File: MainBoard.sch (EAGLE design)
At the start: 47 parts, among them U1 STM32F10XRXT6, X1 53261-03, X2 53261-03, X3 53261-03, X4 53261-03, Y1 8MHz, Y2 32.768kHz

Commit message: płytka
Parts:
- removed C1, C14, C2, C3, C4: 100n, rcl:C-EUC0805
- removed C6: 10u, rcl:CPOL-EUSMCA
- removed ETRX357: ETRX357HR, etrx357_logical:ETRX357HR
- removed G1: CR2032V, battery:CR2032V
- removed SW1: (no value), SparkFun-Electromechanical:SW_DIP-2
- removed X1, X2, X3, X4: 53261-03, con-molex:53261-03
- added C22: (no value), rcl:C-EUC0805
- added IC3: (no value), SparkFun-PowerIC:V_REG_LM1117SOT223
- added JP1: (no value), SparkFun-Connectors:M06LONGPADS
- added JP2, JP3: M05X2SHD, SparkFun-Connectors:M05X2SHD
- added JP4: (no value), SparkFun-Connectors:M04LONGPADS
- added JP5, JP6, JP7, JP8: (no value), SparkFun-Connectors:M03LONGPADS
- added LED5, LED7, LED8, LED9: (no value), led:LEDCHIPLED_0805
- added R10, R12, R13, R14: (no value), resistor:R-EU_M0805
- C21: value 100n -> (none)
- LED1, LED2, LED3: device SparkFun-LED (1):LED1206 -> led:LEDCHIPLED_0805
- R6, R7, R8: value 220 -> (none); device rcl:R-EU_M0805 -> resistor:R-EU_M0805
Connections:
- removed net N$11: LED2.C, R8.2
- removed net N$9: LED3.C, R6.2
- removed net RXD: ETRX357.PB2
- removed net TXD: ETRX357.PB1
- new net 5V: C21.1, IC3.IN, JP5.1, JP6.1, JP7.1, JP8.1
- new net A1: JP2.7, U1PORTB_H.PB8
- new net A2: JP2.5, U1PORTB_H.PB9
- new net A3: JP2.9, U1PORTB_L.PB6
- new net A4: JP2.2, U1PORTB_L.PB7
- new net A5: JP2.8, U1PORTC_H.PC8
- new net A6: JP2.10, U1PORTC_H.PC9
- new net A7: JP2.4, U1PORTC_L.PC6
- new net A8: JP2.6, U1PORTC_L.PC7
- new net L1: R7.1, U1PORTB_H.PB12
- new net L2: R8.1, U1PORTC_L.PC1
- new net L4: R10.1, U1PORTA_L.PA1
- new net L6: R12.1, U1PORTC_L.PC2
- new net L7: R13.1, U1PORTC_L.PC3
- new net MISO: JP3.9, U1PORTA_L.PA6
- new net MOSI: JP3.10, U1PORTA_L.PA7
- new net N$12: LED7.A, R12.2
- new net N$13: LED8.A, R13.2
- new net N$14: LED9.A, R14.2
- new net REG1: JP5.3, U1PORTA_H.PA8
- new net REG2: JP6.3, U1PORTA_H.PA9
- new net REG3: JP7.3, U1PORTA_H.PA10
- new net REG4: JP8.3, U1PORTA_H.PA11
- new net RX: JP3.5, U1PORTA_L.PA3
- new net SCK: JP3.8, U1PORTA_L.PA5
- new net SWO: JP1.6
- new net TX: JP3.6, U1PORTA_L.PA2
- net 3.3V: now also C22.1, IC3.OUT, IC3.OUT@1, JP1.1, JP2.1, JP3.2, JP4.2, JP4.3, R14.1, R6.1; no longer C1.1, C14.1, C2.1, C21.1, C3.1, C4.1, C6.+, ETRX357.VCC, SW1.3, SW1.4
- net GND: now also C22.2, IC3.ADJ, JP1.3, JP2.3, JP3.1, JP5.2, JP6.2, JP7.2, JP8.2, LED1.C, LED2.C, LED3.C, LED5.C, LED7.C, LED8.C, LED9.C; no longer C1.2, C14.2, C2.2, C3.2, C4.2, C6.-, ETRX357.GND@1, ETRX357.GND@2, ETRX357.GND@3, ETRX357.GND@4, ETRX357.GND@5, ETRX357.GND@6, G1.-, R6.1, R7.1, R8.1
- net N$1: now also JP4.1; no longer SW1.1
- net N$10: now also LED5.A, R10.2; no longer LED1.C, R7.2
- net N$2: now also JP4.4; no longer SW1.2
- net N$6: now also R6.2; no longer ETRX357.PC6
- net N$7: now also R7.2; no longer ETRX357.PC7
- net N$8: now also R8.2; no longer ETRX357.PB7
- net NRST: now also JP1.5
- net SCL: now also U1PORTB_H.PB10
- net SDA: now also U1PORTB_H.PB11
- net SWCLK: now also JP1.2
- net SWDIO: now also JP1.4
- net V_BATT: no longer G1.+
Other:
- note removed: "BATTERY"
- note removed: "ETRX357 ZigBee"
- note removed: "VDD/VSS"
- moved on the sheet: C21, C5, C7, LED1, LED2, LED3, R6, R7, R8, Y1

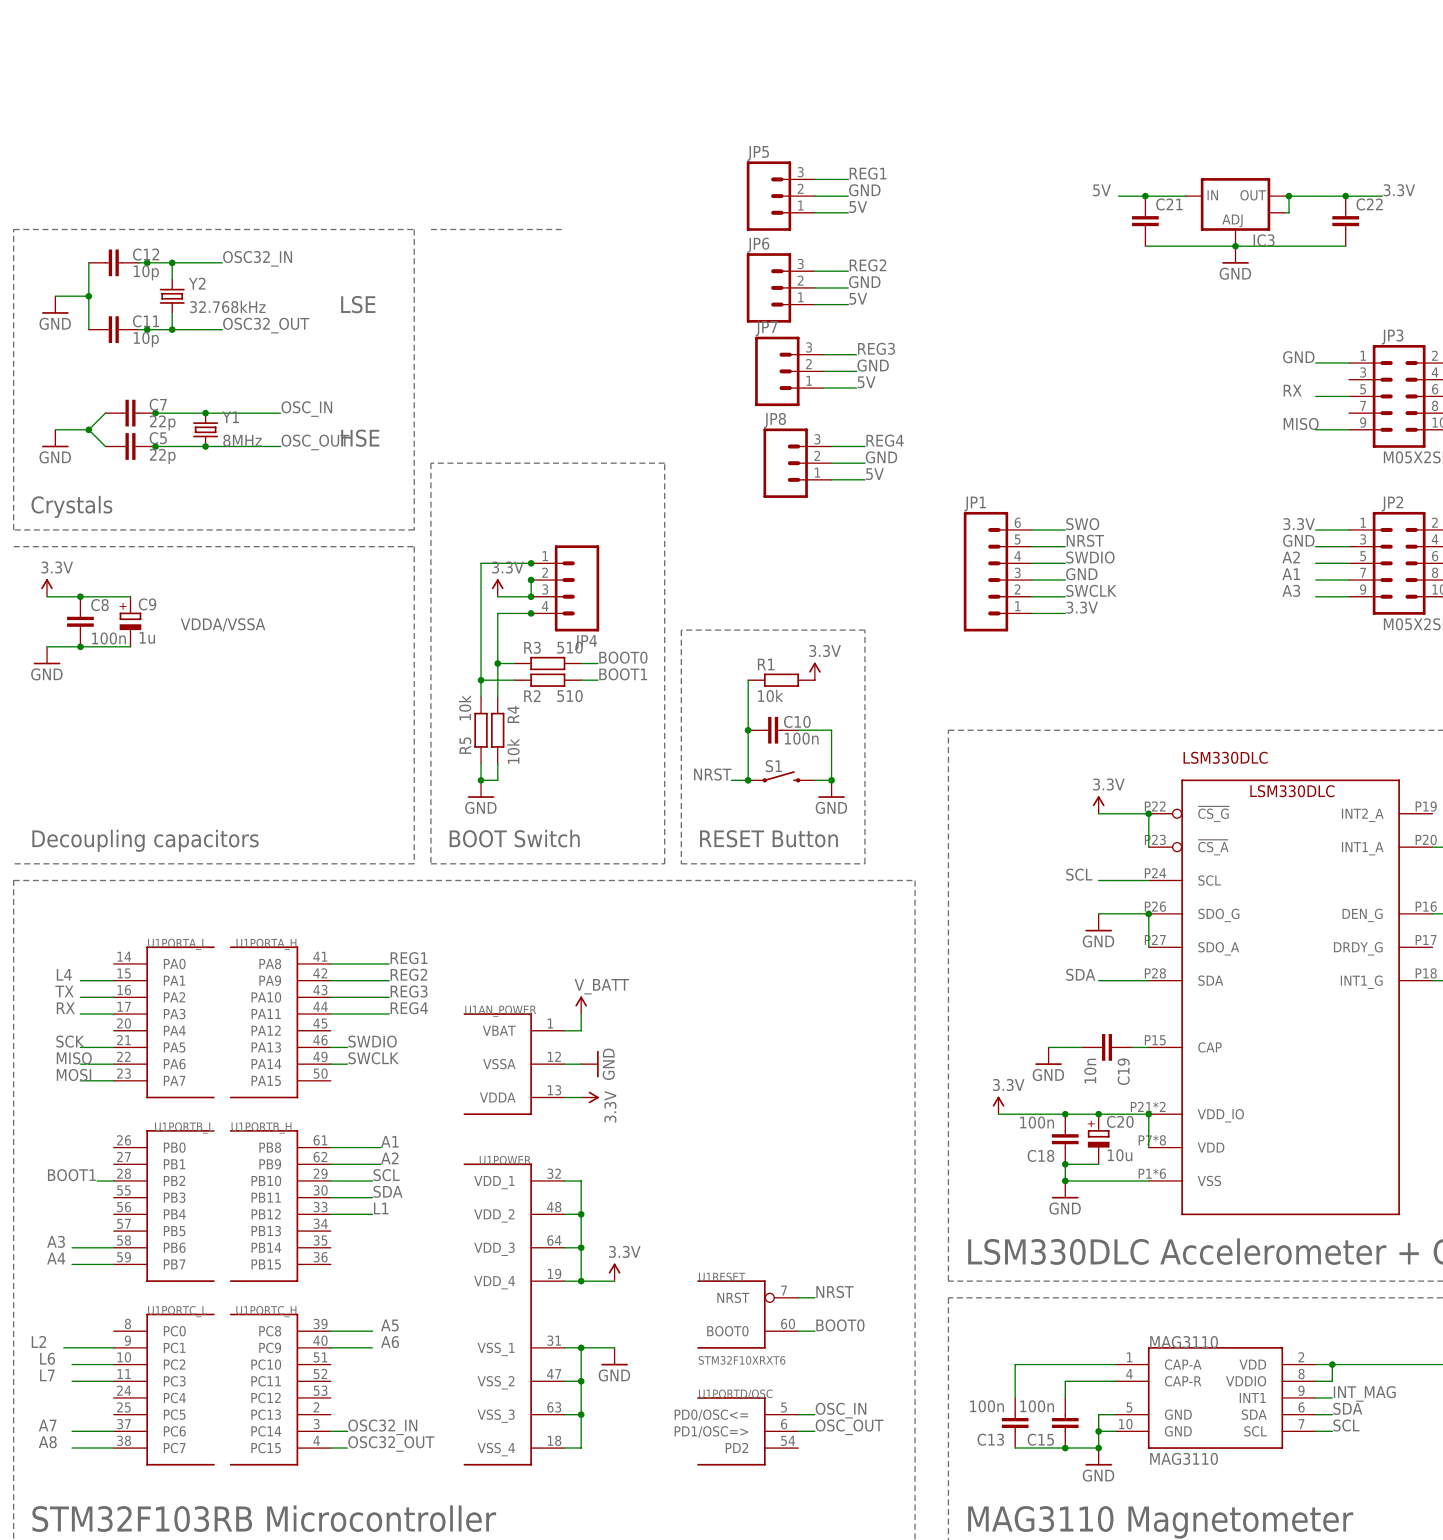
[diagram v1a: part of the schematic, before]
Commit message: buzzer i adc
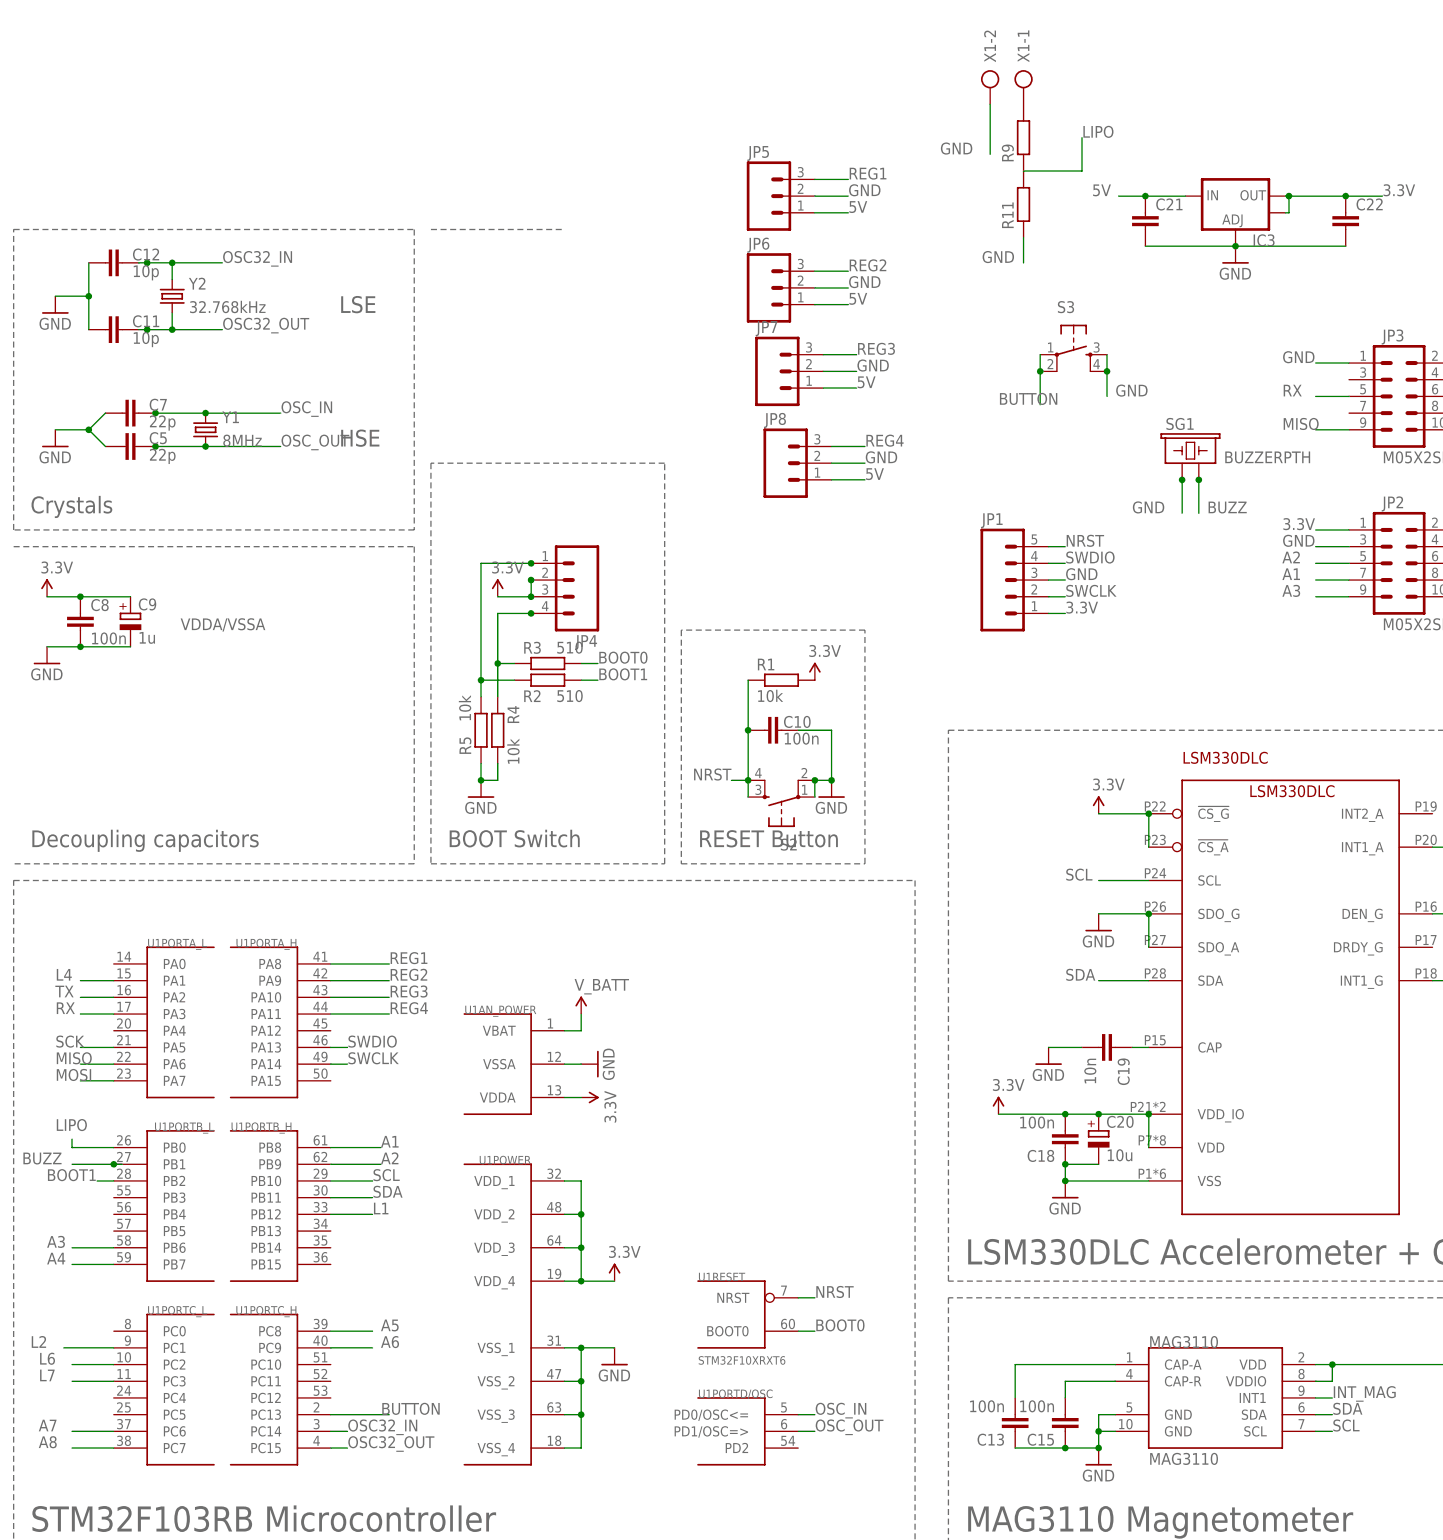
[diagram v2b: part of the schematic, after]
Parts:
- removed S1: SWITCH-MOMENTARY-2-SMD-1101NE, SparkFun-Electromechanical:SWITCH-MOMENTARY-2-SMD-1101NE
- added R11, R9: (no value), resistor:R-EU_M0805
- added S2, S3: (no value), SparkFun-Electromechanical:TAC_SWITCHSMD
- added SG1: BUZZERPTH, SparkFun-Electromechanical:BUZZERPTH
- added X1: (no value), con-ptr500:AK300/2
- JP1: device SparkFun-Connectors:M06LONGPADS -> SparkFun-Connectors:M05PTH_LONGPADS
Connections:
- removed net SWO: JP1.6
- new net BUTTON: S3.1, S3.2, U1PORTC_H.PC13
- new net BUZZ: SG1.2, U1PORTB_L.PB1
- new net LIPO: R11.2, R9.1, U1PORTB_L.PB0
- new net N$19: R9.2, X1-1.KL
- net GND: now also R11.1, S2.1, S2.2, S3.3, S3.4, SG1.1, X1-2.KL; no longer S1.2
- net NRST: now also S2.3, S2.4; no longer S1.1
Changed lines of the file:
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@@
 <part name="C8" library="rcl" deviceset="C-EU" device="C0805" value="100n"/>
 <part name="C9" library="rcl" deviceset="CPOL-EU" device="SMCA" value="1u"/>
-<part name="S1" library="SparkFun-Electromechanical" deviceset="SWITCH-MOMENTARY-2" device="-SMD-1101NE"/>
 <part name="C10" library="rcl" deviceset="C-EU" device="C0805" value="100n"/>
 <part name="GND3" library="SparkFun-Aesthetics" deviceset="GND" device=""/>
@@
 <part name="GND14" library="supply1" deviceset="GND" device=""/>
 <part name="GND15" library="supply1" deviceset="GND" device=""/>
-<part name="JP1" library="SparkFun-Connectors" deviceset="M06" device="LONGPADS"/>
+<part name="JP1" library="SparkFun-Connectors" deviceset="M05" device="PTH_LONGPADS"/>
 <part name="JP2" library="SparkFun-Connectors" deviceset="M05X2" device="SHD" value="M05X2SHD"/>
 <part name="JP3" library="SparkFun-Connectors" deviceset="M05X2" device="SHD" value="M05X2SHD"/>
@@
 <part name="R13" library="resistor" deviceset="R-EU_" device="M0805"/>
 <part name="R14" library="resistor" deviceset="R-EU_" device="M0805"/>
+<part name="S2" library="SparkFun-Electromechanical" deviceset="TAC_SWITCH" device="SMD"/>
+<part name="S3" library="SparkFun-Electromechanical" deviceset="TAC_SWITCH" device="SMD"/>
+<part name="SG1" library="SparkFun-Electromechanical" deviceset="BUZZER" device="PTH"/>
+<part name="X1" library="con-ptr500" deviceset="AK300/2" device=""/>
+<part name="R9" library="resistor" deviceset="R-EU_" device="M0805"/>
+<part name="R11" library="resistor" deviceset="R-EU_" device="M0805"/>
 </parts>
 <sheets>
@@
 <instance part="C8" gate="G$1" x="10.16" y="142.24"/>
 <instance part="C9" gate="G$1" x="17.78" y="142.24"/>
-<instance part="S1" gate="G$1" x="116.84" y="116.84" smashed="yes">
-<attribute name="NAME" x="114.3" y="118.11" size="1.778" layer="95"/>
-</instance>
 <instance part="C10" gate="G$1" x="114.3" y="124.46" smashed="yes" rot="R90">
 <attribute name="NAME" x="117.094" y="124.841" size="1.778" layer="95"/>
@@
 <instance part="R13" gate="G$1" x="241.3" y="162.56"/>
 <instance part="R14" gate="G$1" x="241.3" y="154.94"/>
+<instance part="S2" gate="S" x="116.84" y="114.3" rot="R180"/>
+<instance part="S3" gate="S" x="161.29" y="181.61"/>
+<instance part="SG1" gate="G$1" x="177.8" y="165.1"/>
+<instance part="X1" gate="-1" x="153.67" y="224.79" rot="R270"/>
+<instance part="X1" gate="-2" x="148.59" y="224.79" rot="R270"/>
+<instance part="R9" gate="G$1" x="153.67" y="214.63" rot="R90"/>
+<instance part="R11" gate="G$1" x="153.67" y="204.47" rot="R90"/>
 </instances>
 <busses>
@@
 <segment>
 <pinref part="JP1" gate="G$1" pin="1"/>
-<wire x1="154.94" y1="142.24" x2="160.02" y2="142.24" width="0.1524" layer="91"/>
+<wire x1="157.48" y1="142.24" x2="160.02" y2="142.24" width="0.1524" layer="91"/>
 <label x="160.02" y="142.24" size="1.778" layer="95"/>
 </segment>
@@
 <wire x1="124.46" y1="124.46" x2="124.46" y2="116.84" width="0.1524" layer="91"/>
 <pinref part="GND3" gate="1" pin="GND"/>
-<pinref part="S1" gate="G$1" pin="2"/>
-<pinref part="S1" gate="G$1" pin="2"/>
 <wire x1="121.92" y1="116.84" x2="124.46" y2="116.84" width="0.1524" layer="91"/>
 <junction x="124.46" y="116.84"/>
+<pinref part="S2" gate="S" pin="2"/>
+<pinref part="S2" gate="S" pin="1"/>
+<wire x1="121.92" y1="116.84" x2="121.92" y2="114.3" width="0.1524" layer="91"/>
+<junction x="121.92" y="116.84"/>
 </segment>
 <segment>
@@
 <segment>
 <pinref part="JP1" gate="G$1" pin="3"/>
-<wire x1="154.94" y1="147.32" x2="160.02" y2="147.32" width="0.1524" layer="91"/>
+<wire x1="157.48" y1="147.32" x2="160.02" y2="147.32" width="0.1524" layer="91"/>
 <label x="160.02" y="147.32" size="1.778" layer="95"/>
 </segment>
@@
 <label x="193.04" y="152.4" size="1.778" layer="95"/>
 </segment>
+<segment>
+<pinref part="S3" gate="S" pin="3"/>
+<wire x1="166.37" y1="181.61" x2="166.37" y2="179.07" width="0.1524" layer="91"/>
+<pinref part="S3" gate="S" pin="4"/>
+<junction x="166.37" y="179.07"/>
+<wire x1="166.37" y1="179.07" x2="166.37" y2="175.26" width="0.1524" layer="91"/>
+<label x="167.64" y="175.26" size="1.778" layer="95"/>
+</segment>
+<segment>
+<pinref part="X1" gate="-2" pin="KL"/>
+<wire x1="148.59" y1="219.71" x2="148.59" y2="212.09" width="0.1524" layer="91"/>
+<label x="140.97" y="212.09" size="1.778" layer="95"/>
+</segment>
+<segment>
+<pinref part="R11" gate="G$1" pin="1"/>
+<wire x1="153.67" y1="199.39" x2="153.67" y2="195.58" width="0.1524" layer="91"/>
+<label x="147.32" y="195.58" size="1.778" layer="95"/>
+</segment>
+<segment>
+<pinref part="SG1" gate="G$1" pin="1"/>
+<wire x1="177.8" y1="162.56" x2="177.8" y2="157.48" width="0.1524" layer="91"/>
+<label x="170.18" y="157.48" size="1.778" layer="95"/>
+<junction x="177.8" y="162.56"/>
+</segment>
 </net>
 <net name="SWDIO" class="0">
@@
 <segment>
 <pinref part="JP1" gate="G$1" pin="4"/>
-<wire x1="154.94" y1="149.86" x2="160.02" y2="149.86" width="0.1524" layer="91"/>
+<wire x1="157.48" y1="149.86" x2="160.02" y2="149.86" width="0.1524" layer="91"/>
 <label x="160.02" y="149.86" size="1.778" layer="95"/>
 </segment>
@@
 <segment>
 <pinref part="JP1" gate="G$1" pin="2"/>
-<wire x1="154.94" y1="144.78" x2="160.02" y2="144.78" width="0.1524" layer="91"/>
+<wire x1="157.48" y1="144.78" x2="160.02" y2="144.78" width="0.1524" layer="91"/>
 <label x="160.02" y="144.78" size="1.778" layer="95"/>
 </segment>
@@
 <pinref part="R1" gate="G$1" pin="1"/>
 <wire x1="111.76" y1="132.08" x2="111.76" y2="124.46" width="0.1524" layer="91"/>
-<pinref part="S1" gate="G$1" pin="1"/>
 <wire x1="111.76" y1="116.84" x2="109.22" y2="116.84" width="0.1524" layer="91"/>
 <label x="109.22" y="116.84" size="1.778" layer="95" rot="MR0"/>
 <wire x1="111.76" y1="124.46" x2="111.76" y2="116.84" width="0.1524" layer="91"/>
 <junction x="111.76" y="124.46"/>
+<pinref part="S2" gate="S" pin="4"/>
 <junction x="111.76" y="116.84"/>
+<pinref part="S2" gate="S" pin="3"/>
+<wire x1="111.76" y1="116.84" x2="111.76" y2="114.3" width="0.1524" layer="91"/>
 </segment>
 <segment>
@@
 <segment>
 <pinref part="JP1" gate="G$1" pin="5"/>
-<wire x1="154.94" y1="152.4" x2="160.02" y2="152.4" width="0.1524" layer="91"/>
+<wire x1="157.48" y1="152.4" x2="160.02" y2="152.4" width="0.1524" layer="91"/>
 <label x="160.02" y="152.4" size="1.778" layer="95"/>
 </segment>
@@
 </segment>
 </net>
-<net name="SWO" class="0">
-<segment>
-<pinref part="JP1" gate="G$1" pin="6"/>
-<wire x1="154.94" y1="154.94" x2="160.02" y2="154.94" width="0.1524" layer="91"/>
-<label x="160.02" y="154.94" size="1.778" layer="95"/>
-</segment>
-</net>
 <net name="A4" class="0">
 <segment>
@@
 </segment>
 </net>
+<net name="BUTTON" class="0">
+<segment>
+<pinref part="S3" gate="S" pin="1"/>
+<wire x1="156.21" y1="181.61" x2="156.21" y2="179.07" width="0.1524" layer="91"/>
+<pinref part="S3" gate="S" pin="2"/>
+<junction x="156.21" y="179.07"/>
+<wire x1="156.21" y1="179.07" x2="156.21" y2="173.99" width="0.1524" layer="91"/>
+<label x="149.86" y="173.99" size="1.778" layer="95"/>
+</segment>
+<segment>
+<pinref part="U1" gate="PORTC_H" pin="PC13"/>
+<wire x1="48.26" y1="20.32" x2="57.15" y2="20.32" width="0.1524" layer="91"/>
+<label x="55.88" y="20.32" size="1.778" layer="95"/>
+</segment>
+</net>
+<net name="N$19" class="0">
+<segment>
+<pinref part="X1" gate="-1" pin="KL"/>
+<pinref part="R9" gate="G$1" pin="2"/>
+</segment>
+</net>
+<net name="LIPO" class="0">
+<segment>
+<pinref part="R9" gate="G$1" pin="1"/>
+<pinref part="R11" gate="G$1" pin="2"/>
+<wire x1="153.67" y1="209.55" x2="162.56" y2="209.55" width="0.1524" layer="91"/>
+<wire x1="162.56" y1="209.55" x2="162.56" y2="214.63" width="0.1524" layer="91"/>
+<label x="162.56" y="214.63" size="1.778" layer="95"/>
+</segment>
+<segment>
+<pinref part="U1" gate="PORTB_L" pin="PB0"/>
+<wire x1="15.24" y1="60.96" x2="8.89" y2="60.96" width="0.1524" layer="91"/>
+<wire x1="8.89" y1="60.96" x2="8.89" y2="62.23" width="0.1524" layer="91"/>
+<label x="6.35" y="63.5" size="1.778" layer="95"/>
+</segment>
+</net>
+<net name="BUZZ" class="0">
+<segment>
+<pinref part="SG1" gate="G$1" pin="2"/>
+<wire x1="180.34" y1="162.56" x2="180.34" y2="157.48" width="0.1524" layer="91"/>
+<label x="181.61" y="157.48" size="1.778" layer="95"/>
+<junction x="180.34" y="162.56"/>
+</segment>
+<segment>
+<wire x1="16.51" y1="58.42" x2="15.24" y2="58.42" width="0.1524" layer="91"/>
+<label x="1.27" y="58.42" size="1.778" layer="95"/>
+<pinref part="U1" gate="PORTB_L" pin="PB1"/>
+<junction x="15.24" y="58.42"/>
+<wire x1="15.24" y1="58.42" x2="8.89" y2="58.42" width="0.1524" layer="91"/>
+</segment>
+</net>
